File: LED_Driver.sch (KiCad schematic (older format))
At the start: 0 parts

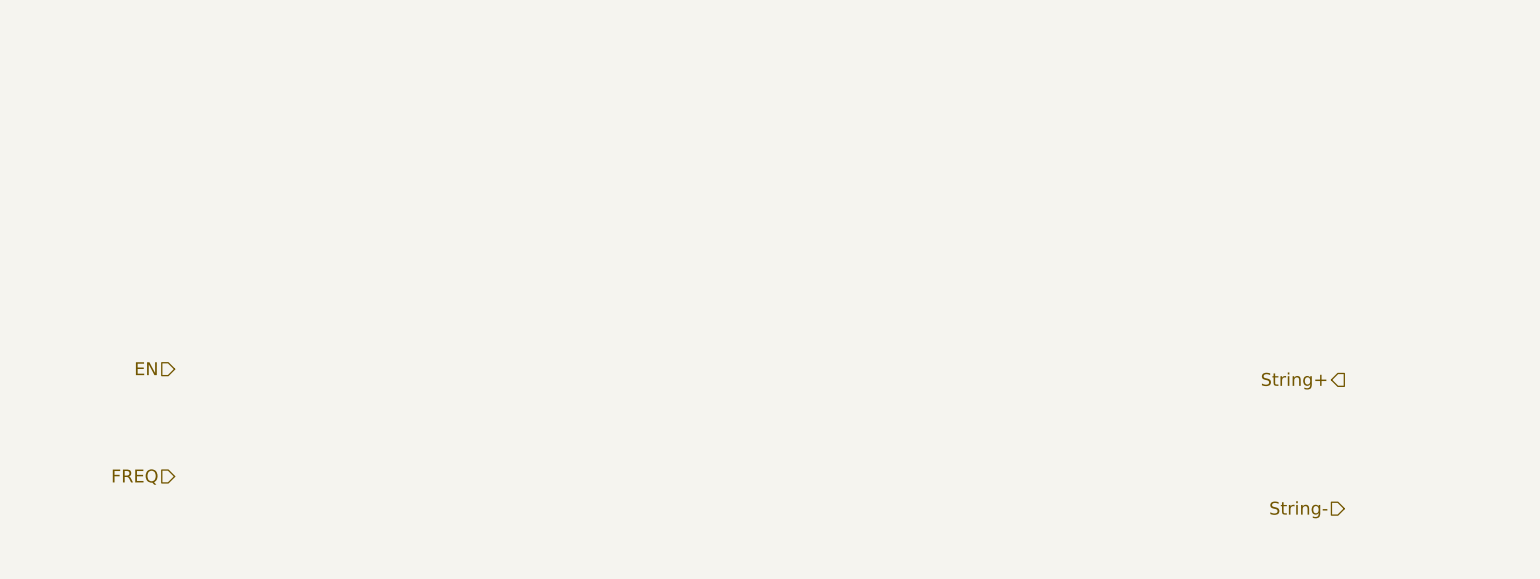
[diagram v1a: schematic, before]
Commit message: Current driver refactoring, LED module, Arduino
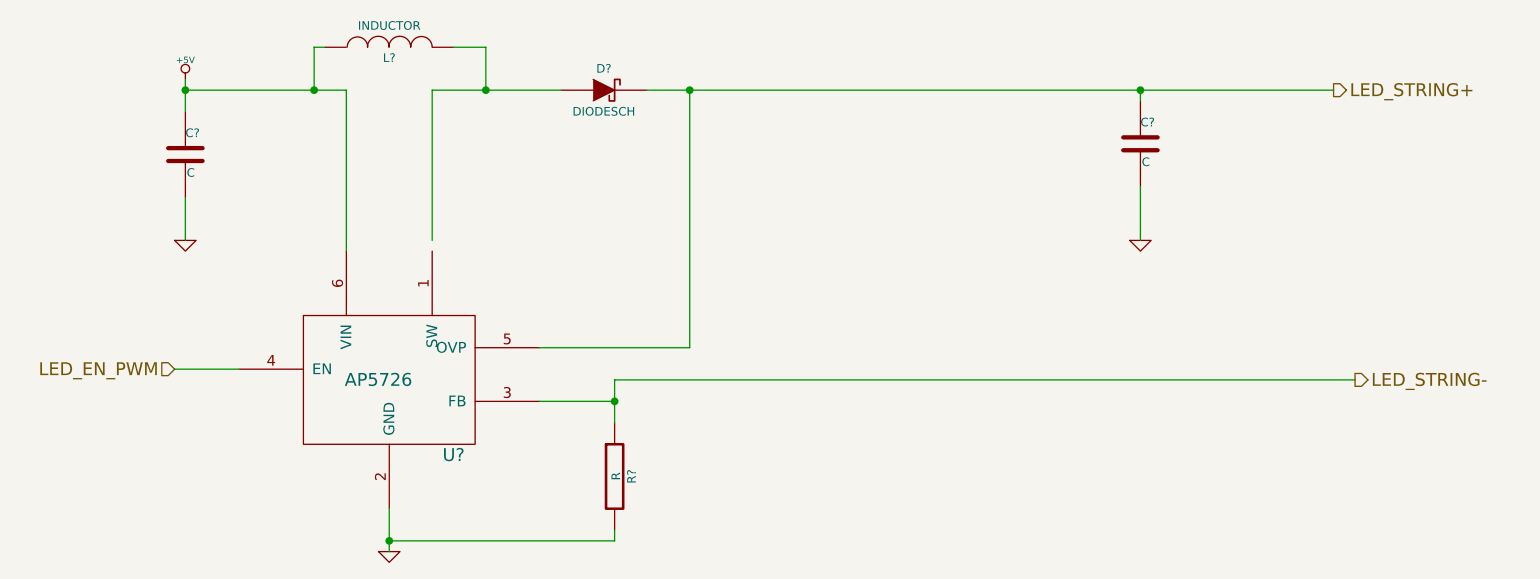
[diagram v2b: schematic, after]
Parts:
- added C? (x2): C, ~, symbol C
- added D?: DIODESCH, ~, symbol DIODESCH
- added L?: INDUCTOR, ~, symbol INDUCTOR
- added R?: R, ~, symbol R
- added U?: AP5726, symbol AP5726
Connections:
- net labels added: +5V, GND, LED_EN_PWM, LED_STRING+, LED_STRING-
- net labels removed: EN, FREQ, String+, String-
- wire segments 0 -> 22
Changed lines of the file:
@@
 $Descr A4 11693 8268
 encoding utf-8
-Sheet 6 9
+Sheet 5 9
 Title ""
 Date "9 feb 2014"
@@
 $EndDescr
 Text HLabel 2400 2700 0    60   Input ~ 0
-EN
-Text HLabel 2400 3200 0    60   Input ~ 0
-FREQ
-Text HLabel 7850 2750 0    60   Output ~ 0
-String+
-Text HLabel 7850 3350 0    60   Input ~ 0
-String-
+LED_EN_PWM
+Text HLabel 7800 1400 2    60   Output ~ 0
+LED_STRING+
+Text HLabel 7900 2750 2    60   Output ~ 0
+LED_STRING-
+$Comp
+L AP5726 U?
+U 1 1 52F709C9
+P 3400 2700
+F 0 "U?" H 3700 2300 60  0000 C CNN
+F 1 "AP5726" H 3350 2650 60  0000 C CNN
+F 2 "" H 2600 2300 60  0000 C CNN
+F 3 "" H 2600 2300 60  0000 C CNN
+	1    3400 2700
+	1    0    0    -1
+$EndComp
+Wire Wire Line
+	2400 2700 2700 2700
+$Comp
+L +5V #PWR?
+U 1 1 52F70E27
+P 2450 1350
+F 0 "#PWR?" H 2450 1440 20  0001 C CNN
+F 1 "+5V" H 2450 1440 30  0000 C CNN
+F 2 "" H 2450 1350 60  0000 C CNN
+F 3 "" H 2450 1350 60  0000 C CNN
+	1    2450 1350
+	1    0    0    -1
+$EndComp
+$Comp
+L GND #PWR?
+U 1 1 52F70E36
+P 6900 2100
+F 0 "#PWR?" H 6900 2100 30  0001 C CNN
+F 1 "GND" H 6900 2030 30  0001 C CNN
+F 2 "" H 6900 2100 60  0000 C CNN
+F 3 "" H 6900 2100 60  0000 C CNN
+	1    6900 2100
+	1    0    0    -1
+$EndComp
+$Comp
+L GND #PWR?
+U 1 1 52F70E4F
+P 2450 2100
+F 0 "#PWR?" H 2450 2100 30  0001 C CNN
+F 1 "GND" H 2450 2030 30  0001 C CNN
+F 2 "" H 2450 2100 60  0000 C CNN
+F 3 "" H 2450 2100 60  0000 C CNN
+	1    2450 2100
+	1    0    0    -1
+$EndComp
+$Comp
+L C C?
+U 1 1 52F70E5A
+P 2450 1700
+F 0 "C?" H 2450 1800 40  0000 L CNN
+F 1 "C" H 2456 1615 40  0000 L CNN
+F 2 "~" H 2488 1550 30  0000 C CNN
+F 3 "~" H 2450 1700 60  0000 C CNN
+	1    2450 1700
+	1    0    0    -1
+$EndComp
+Wire Wire Line
+	2450 1350 2450 1500
+Wire Wire Line
+	2450 1900 2450 2100
+Wire Wire Line
+	2450 1400 3200 1400
+Wire Wire Line
+	3200 1400 3200 2150
+Connection ~ 2450 1400
+$Comp
+L C C?
+U 1 1 52F70E9B
+P 6900 1650
+F 0 "C?" H 6900 1750 40  0000 L CNN
+F 1 "C" H 6906 1565 40  0000 L CNN
+F 2 "~" H 6938 1500 30  0000 C CNN
+F 3 "~" H 6900 1650 60  0000 C CNN
+	1    6900 1650
+	1    0    0    -1
+$EndComp
+$Comp
+L INDUCTOR L?
+U 1 1 52F70EA3
+P 3400 1200
+F 0 "L?" V 3350 1200 40  0000 C CNN
+F 1 "INDUCTOR" V 3500 1200 40  0000 C CNN
+F 2 "~" H 3400 1200 60  0000 C CNN
+F 3 "~" H 3400 1200 60  0000 C CNN
+	1    3400 1200
+	0    -1   -1   0
+$EndComp
+Wire Wire Line
+	3100 1200 3050 1200
+Wire Wire Line
+	3050 1200 3050 1400
+Connection ~ 3050 1400
+Wire Wire Line
+	3600 2100 3600 1400
+Wire Wire Line
+	3600 1400 4200 1400
+Wire Wire Line
+	3700 1200 3850 1200
+Wire Wire Line
+	3850 1200 3850 1400
+Connection ~ 3850 1400
+$Comp
+L DIODESCH D?
+U 1 1 52F70EE8
+P 4400 1400
+F 0 "D?" H 4400 1500 40  0000 C CNN
+F 1 "DIODESCH" H 4400 1300 40  0000 C CNN
+F 2 "~" H 4400 1400 60  0000 C CNN
+F 3 "~" H 4400 1400 60  0000 C CNN
+	1    4400 1400
+	1    0    0    -1
+$EndComp
+Wire Wire Line
+	4600 1400 7800 1400
+Wire Wire Line
+	6900 1400 6900 1450
+Wire Wire Line
+	6900 1850 6900 2100
+$Comp
+L R R?
+U 1 1 52F70F4A
+P 4450 3200
+F 0 "R?" V 4530 3200 40  0000 C CNN
+F 1 "R" V 4457 3201 40  0000 C CNN
+F 2 "~" V 4380 3200 30  0000 C CNN
+F 3 "~" H 4450 3200 30  0000 C CNN
+	1    4450 3200
+	1    0    0    -1
+$EndComp
+Wire Wire Line
+	4100 2850 4450 2850
+Wire Wire Line
+	4450 2750 4450 2950
+$Comp
+L GND #PWR?
+U 1 1 52F70F6C
+P 3400 3550
+F 0 "#PWR?" H 3400 3550 30  0001 C CNN
+F 1 "GND" H 3400 3480 30  0001 C CNN
+F 2 "" H 3400 3550 60  0000 C CNN
+F 3 "" H 3400 3550 60  0000 C CNN
+	1    3400 3550
+	1    0    0    -1
+$EndComp
+Wire Wire Line
+	3400 3350 3400 3550
+Wire Wire Line
+	4450 3450 4450 3500
+Wire Wire Line
+	4450 3500 3400 3500
+Connection ~ 3400 3500
+Wire Wire Line
+	7900 2750 4450 2750
+Connection ~ 4450 2850
+Wire Wire Line
+	4100 2600 4800 2600
+Wire Wire Line
+	4800 2600 4800 1400
+Connection ~ 4800 1400
+Connection ~ 6900 1400
 $EndSCHEMATC

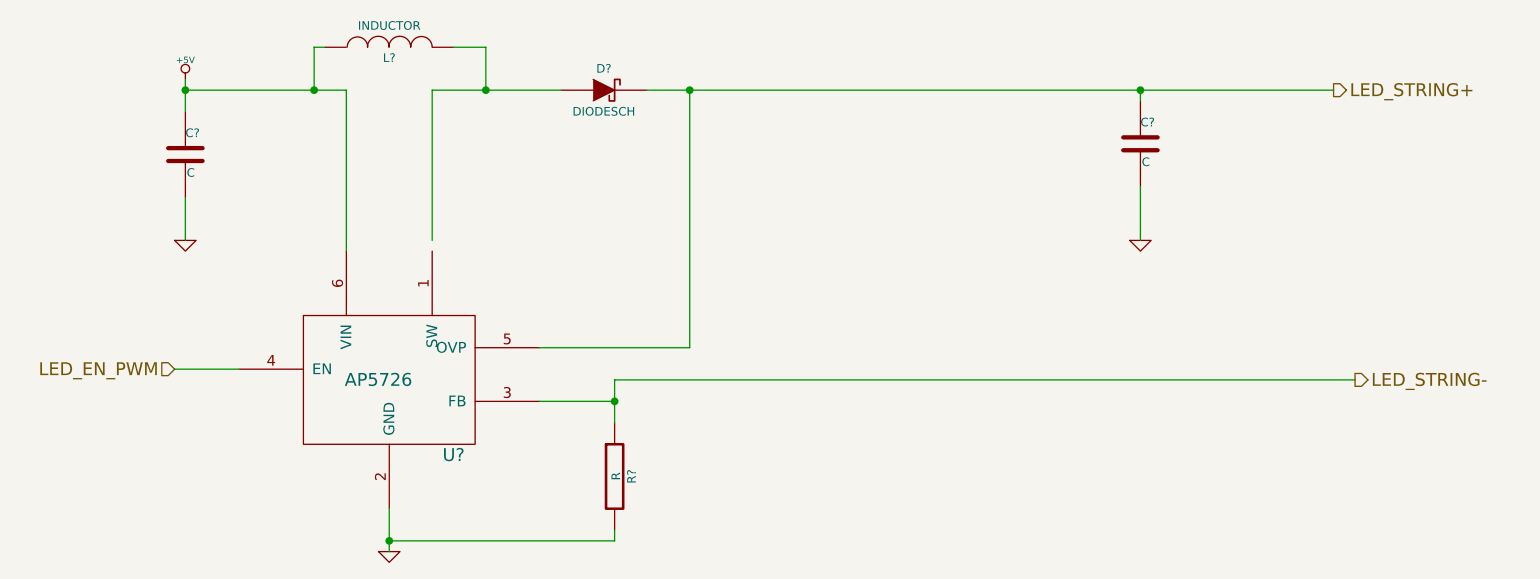
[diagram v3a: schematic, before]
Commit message: Relay module association and placement
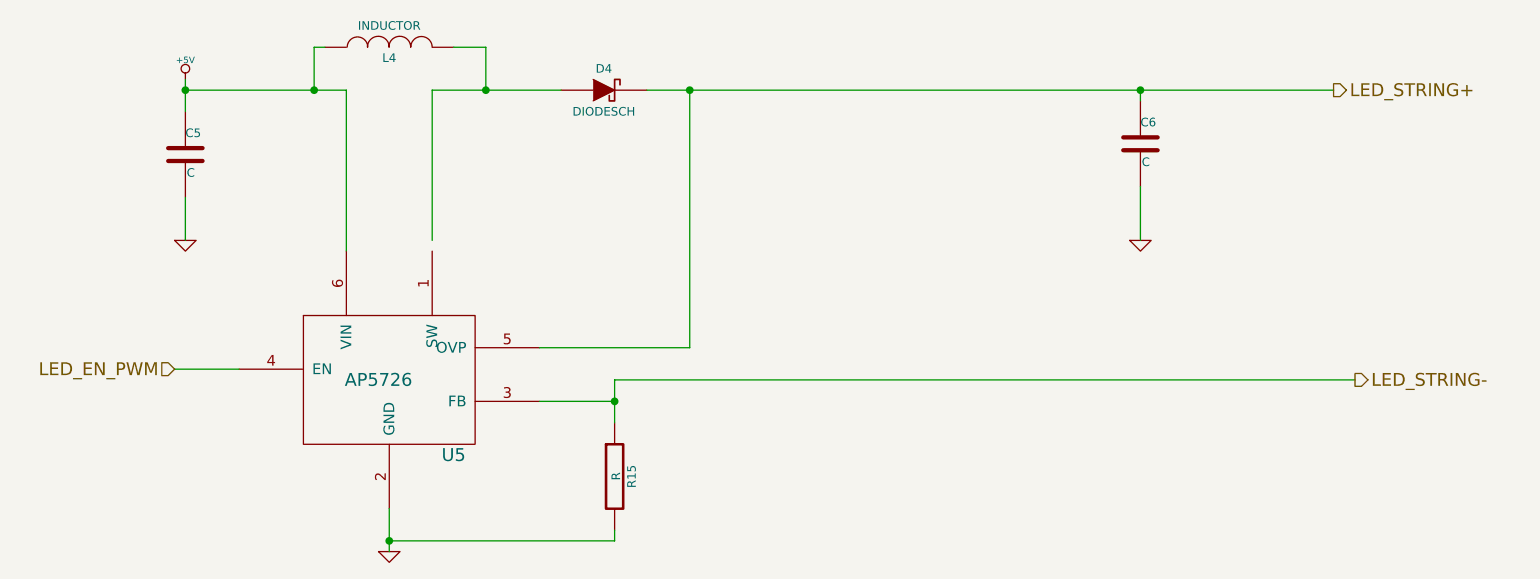
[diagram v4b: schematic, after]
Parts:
- gave numbers to parts that had none: 6
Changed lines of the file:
@@
 Sheet 5 9
 Title ""
-Date "18 feb 2014"
+Date "20 feb 2014"
 Rev ""
 Comp ""
@@
 LED_STRING-
 $Comp
-L AP5726 U?
+L AP5726 U5
 U 1 1 52F709C9
 P 3400 2700
-F 0 "U?" H 3700 2300 60  0000 C CNN
+F 0 "U5" H 3700 2300 60  0000 C CNN
 F 1 "AP5726" H 3350 2650 60  0000 C CNN
 F 2 "" H 2600 2300 60  0000 C CNN
@@
 	2400 2700 2700 2700
 $Comp
-L +5V #PWR?
+L +5V #PWR025
 U 1 1 52F70E27
 P 2450 1350
-F 0 "#PWR?" H 2450 1440 20  0001 C CNN
+F 0 "#PWR025" H 2450 1440 20  0001 C CNN
 F 1 "+5V" H 2450 1440 30  0000 C CNN
 F 2 "" H 2450 1350 60  0000 C CNN
@@
 $EndComp
 $Comp
-L GND #PWR?
+L GND #PWR026
 U 1 1 52F70E36
 P 6900 2100
-F 0 "#PWR?" H 6900 2100 30  0001 C CNN
+F 0 "#PWR026" H 6900 2100 30  0001 C CNN
 F 1 "GND" H 6900 2030 30  0001 C CNN
 F 2 "" H 6900 2100 60  0000 C CNN
@@
 $EndComp
 $Comp
-L GND #PWR?
+L GND #PWR027
 U 1 1 52F70E4F
 P 2450 2100
-F 0 "#PWR?" H 2450 2100 30  0001 C CNN
+F 0 "#PWR027" H 2450 2100 30  0001 C CNN
 F 1 "GND" H 2450 2030 30  0001 C CNN
 F 2 "" H 2450 2100 60  0000 C CNN
@@
 $EndComp
 $Comp
-L C C?
+L C C5
 U 1 1 52F70E5A
 P 2450 1700
-F 0 "C?" H 2450 1800 40  0000 L CNN
+F 0 "C5" H 2450 1800 40  0000 L CNN
 F 1 "C" H 2456 1615 40  0000 L CNN
 F 2 "~" H 2488 1550 30  0000 C CNN
@@
 Connection ~ 2450 1400
 $Comp
-L C C?
+L C C6
 U 1 1 52F70E9B
 P 6900 1650
-F 0 "C?" H 6900 1750 40  0000 L CNN
+F 0 "C6" H 6900 1750 40  0000 L CNN
 F 1 "C" H 6906 1565 40  0000 L CNN
 F 2 "~" H 6938 1500 30  0000 C CNN
@@
 $EndComp
 $Comp
-L INDUCTOR L?
+L INDUCTOR L4
 U 1 1 52F70EA3
 P 3400 1200
-F 0 "L?" V 3350 1200 40  0000 C CNN
+F 0 "L4" V 3350 1200 40  0000 C CNN
 F 1 "INDUCTOR" V 3500 1200 40  0000 C CNN
 F 2 "~" H 3400 1200 60  0000 C CNN
@@
 Connection ~ 3850 1400
 $Comp
-L DIODESCH D?
+L DIODESCH D4
 U 1 1 52F70EE8
 P 4400 1400
-F 0 "D?" H 4400 1500 40  0000 C CNN
+F 0 "D4" H 4400 1500 40  0000 C CNN
 F 1 "DIODESCH" H 4400 1300 40  0000 C CNN
 F 2 "~" H 4400 1400 60  0000 C CNN
@@
 	6900 1850 6900 2100
 $Comp
-L R R?
+L R R15
 U 1 1 52F70F4A
 P 4450 3200
-F 0 "R?" V 4530 3200 40  0000 C CNN
+F 0 "R15" V 4530 3200 40  0000 C CNN
 F 1 "R" V 4457 3201 40  0000 C CNN
 F 2 "~" V 4380 3200 30  0000 C CNN
@@
 	4450 2750 4450 2950
 $Comp
-L GND #PWR?
+L GND #PWR028
 U 1 1 52F70F6C
 P 3400 3550
-F 0 "#PWR?" H 3400 3550 30  0001 C CNN
+F 0 "#PWR028" H 3400 3550 30  0001 C CNN
 F 1 "GND" H 3400 3480 30  0001 C CNN
 F 2 "" H 3400 3550 60  0000 C CNN
